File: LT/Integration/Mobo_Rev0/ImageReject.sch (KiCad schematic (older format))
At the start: 6 parts

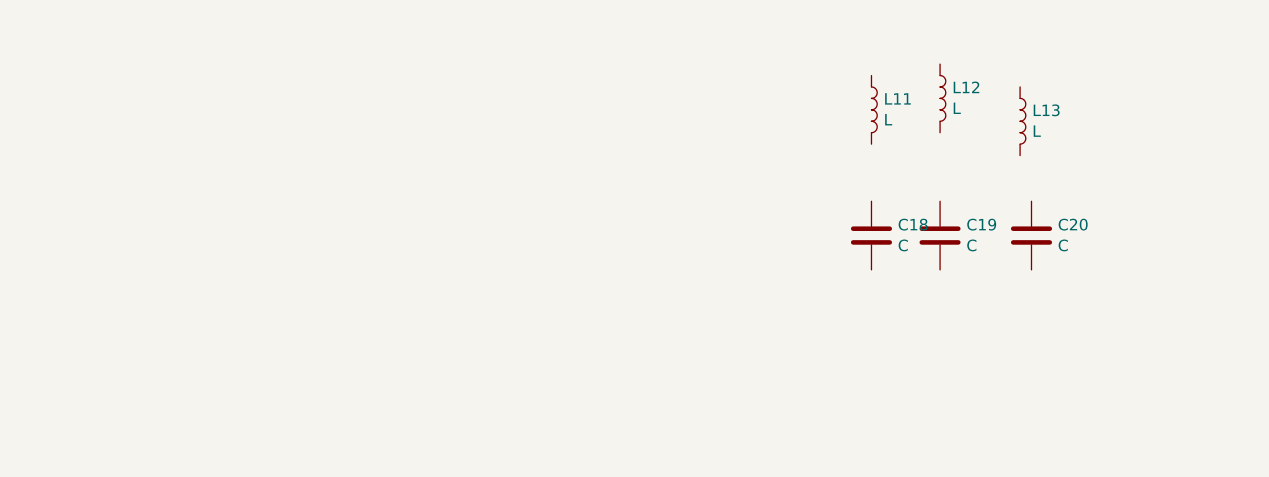
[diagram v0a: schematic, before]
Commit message: I uploaded the schematics for the receiving stage into their respective hierarchial sheets and have begun the integration of the received stage
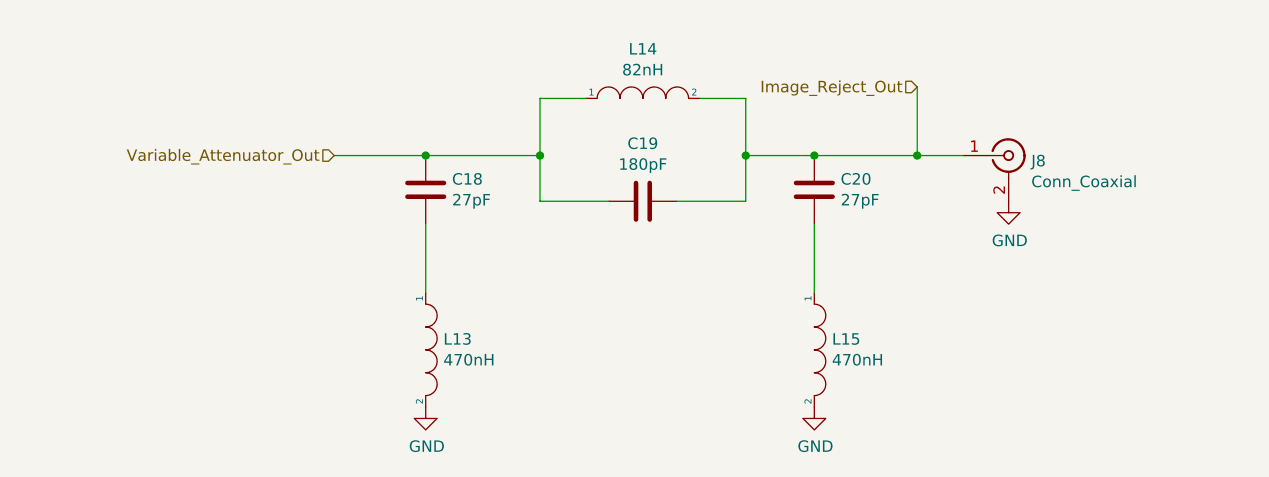
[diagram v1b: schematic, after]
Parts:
- removed L11, L12, L13: L, Inductor_SMD:L_0805_2012Metric, symbol Device:L
- added J8: Conn_Coaxial, Connector_Coaxial:SMA_Molex_73251-1153_EdgeMount_Horizontal, symbol Connector:Conn_Coaxial
- added L13, L15: 470nH, Inductor_SMD:L_0805_2012Metric_Pad1.15x1.40mm_HandSolder, symbol pspice:INDUCTOR
- added L14: 82nH, Inductor_SMD:L_0805_2012Metric_Pad1.15x1.40mm_HandSolder, symbol pspice:INDUCTOR
- C18, C20: value C -> 27pF; footprint Capacitor_SMD:C_0805_2012Metric -> Capacitor_SMD:C_0805_2012Metric_Pad1.15x1.40mm_HandSolder
- C19: value C -> 180pF; footprint Capacitor_SMD:C_0805_2012Metric -> Capacitor_SMD:C_0805_2012Metric_Pad1.15x1.40mm_HandSolder
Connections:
- net Variable_Attenuator_Out: now reaches C18.1
- net Variable_Attenuator_Out: now also C19.2, L14.1
- net at C18.2: now also L13.1
- net Image_Reject_Out: now reaches C19.1
- net Image_Reject_Out: now also C20.1, J8.1 (In), L14.2
- net at C20.2: now also L15.1
- new net GND: J8.2 (Ext), L13.2, L15.2
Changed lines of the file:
@@
 $EndDescr
 $Comp
-L Device:L L11
-U 1 1 5E4B3625
-P 4150 1900
-F 0 "L11" H 4203 1946 50  0000 L CNN
-F 1 "L" H 4203 1855 50  0000 L CNN
-F 2 "Inductor_SMD:L_0805_2012Metric" H 4150 1900 50  0001 C CNN
-F 3 "~" H 4150 1900 50  0001 C CNN
-	1    4150 1900
+L Device:C C18
+U 1 1 5CAD0F21
+P 2200 2250
+F 0 "C18" H 2315 2296 50  0000 L CNN
+F 1 "27pF" H 2315 2205 50  0000 L CNN
+F 2 "Capacitor_SMD:C_0805_2012Metric_Pad1.15x1.40mm_HandSolder" H 2238 2100 50  0001 C CNN
+F 3 "~" H 2200 2250 50  0001 C CNN
+	1    2200 2250
 	1    0    0    -1
 $EndComp
 $Comp
-L Device:L L12
-U 1 1 5E4B3675
-P 4450 1850
-F 0 "L12" H 4503 1896 50  0000 L CNN
-F 1 "L" H 4503 1805 50  0000 L CNN
-F 2 "Inductor_SMD:L_0805_2012Metric" H 4450 1850 50  0001 C CNN
-F 3 "~" H 4450 1850 50  0001 C CNN
-	1    4450 1850
-	1    0    0    -1
-$EndComp
-$Comp
-L Device:L L13
-U 1 1 5E4B36B4
-P 4800 1950
-F 0 "L13" H 4853 1996 50  0000 L CNN
-F 1 "L" H 4853 1905 50  0000 L CNN
-F 2 "Inductor_SMD:L_0805_2012Metric" H 4800 1950 50  0001 C CNN
-F 3 "~" H 4800 1950 50  0001 C CNN
-	1    4800 1950
-	1    0    0    -1
-$EndComp
-$Comp
-L Device:C C18
-U 1 1 5E4B36FA
-P 4150 2450
-F 0 "C18" H 4265 2496 50  0000 L CNN
-F 1 "C" H 4265 2405 50  0000 L CNN
-F 2 "Capacitor_SMD:C_0805_2012Metric" H 4188 2300 50  0001 C CNN
-F 3 "~" H 4150 2450 50  0001 C CNN
-	1    4150 2450
+L Device:C C20
+U 1 1 5CAD104E
+P 3900 2250
+F 0 "C20" H 4015 2296 50  0000 L CNN
+F 1 "27pF" H 4015 2205 50  0000 L CNN
+F 2 "Capacitor_SMD:C_0805_2012Metric_Pad1.15x1.40mm_HandSolder" H 3938 2100 50  0001 C CNN
+F 3 "~" H 3900 2250 50  0001 C CNN
+	1    3900 2250
 	1    0    0    -1
 $EndComp
 $Comp
 L Device:C C19
-U 1 1 5E4B3741
-P 4450 2450
-F 0 "C19" H 4565 2496 50  0000 L CNN
-F 1 "C" H 4565 2405 50  0000 L CNN
-F 2 "Capacitor_SMD:C_0805_2012Metric" H 4488 2300 50  0001 C CNN
-F 3 "~" H 4450 2450 50  0001 C CNN
-	1    4450 2450
+U 1 1 5CAD10AE
+P 3150 2300
+F 0 "C19" V 2898 2300 50  0000 C CNN
+F 1 "180pF" V 2989 2300 50  0000 C CNN
+F 2 "Capacitor_SMD:C_0805_2012Metric_Pad1.15x1.40mm_HandSolder" H 3188 2150 50  0001 C CNN
+F 3 "~" H 3150 2300 50  0001 C CNN
+	1    3150 2300
+	0    1    1    0
+$EndComp
+$Comp
+L pspice:INDUCTOR L14
+U 1 1 5CAD1149
+P 3150 1850
+F 0 "L14" H 3150 2065 50  0000 C CNN
+F 1 "82nH" H 3150 1974 50  0000 C CNN
+F 2 "Inductor_SMD:L_0805_2012Metric_Pad1.15x1.40mm_HandSolder" H 3150 1850 50  0001 C CNN
+F 3 "~" H 3150 1850 50  0001 C CNN
+	1    3150 1850
 	1    0    0    -1
 $EndComp
 $Comp
-L Device:C C20
-U 1 1 5E4B3780
-P 4850 2450
-F 0 "C20" H 4965 2496 50  0000 L CNN
-F 1 "C" H 4965 2405 50  0000 L CNN
-F 2 "Capacitor_SMD:C_0805_2012Metric" H 4888 2300 50  0001 C CNN
-F 3 "~" H 4850 2450 50  0001 C CNN
-	1    4850 2450
+L pspice:INDUCTOR L13
+U 1 1 5CAD11AF
+P 2200 2950
+F 0 "L13" V 2154 3027 50  0000 L CNN
+F 1 "470nH" V 2245 3027 50  0000 L CNN
+F 2 "Inductor_SMD:L_0805_2012Metric_Pad1.15x1.40mm_HandSolder" H 2200 2950 50  0001 C CNN
+F 3 "~" H 2200 2950 50  0001 C CNN
+	1    2200 2950
+	0    1    1    0
+$EndComp
+$Comp
+L pspice:INDUCTOR L15
+U 1 1 5CAD1219
+P 3900 2950
+F 0 "L15" V 3854 3027 50  0000 L CNN
+F 1 "470nH" V 3945 3027 50  0000 L CNN
+F 2 "Inductor_SMD:L_0805_2012Metric_Pad1.15x1.40mm_HandSolder" H 3900 2950 50  0001 C CNN
+F 3 "~" H 3900 2950 50  0001 C CNN
+	1    3900 2950
+	0    1    1    0
+$EndComp
+Wire Wire Line
+	2200 2400 2200 2700
+Wire Wire Line
+	3900 2400 3900 2700
+Wire Wire Line
+	2200 2100 2700 2100
+Wire Wire Line
+	2700 2100 2700 1850
+Wire Wire Line
+	2700 1850 2900 1850
+Wire Wire Line
+	2700 2100 2700 2300
+Wire Wire Line
+	2700 2300 3000 2300
+Connection ~ 2700 2100
+Wire Wire Line
+	3300 2300 3600 2300
+Wire Wire Line
+	3600 2300 3600 2100
+Wire Wire Line
+	3600 1850 3400 1850
+Wire Wire Line
+	3600 2100 3900 2100
+Connection ~ 3600 2100
+Wire Wire Line
+	3600 2100 3600 1850
+$Comp
+L power:GND #PWR012
+U 1 1 5CAD1657
+P 3900 3200
+F 0 "#PWR012" H 3900 2950 50  0001 C CNN
+F 1 "GND" H 3905 3027 50  0000 C CNN
+F 2 "" H 3900 3200 50  0001 C CNN
+F 3 "" H 3900 3200 50  0001 C CNN
+	1    3900 3200
 	1    0    0    -1
 $EndComp
+$Comp
+L power:GND #PWR011
+U 1 1 5CAD1681
+P 2200 3200
+F 0 "#PWR011" H 2200 2950 50  0001 C CNN
+F 1 "GND" H 2205 3027 50  0000 C CNN
+F 2 "" H 2200 3200 50  0001 C CNN
+F 3 "" H 2200 3200 50  0001 C CNN
+	1    2200 3200
+	1    0    0    -1
+$EndComp
+Connection ~ 2200 2100
+$Comp
+L Connector:Conn_Coaxial J8
+U 1 1 5CAD1901
+P 4750 2100
+F 0 "J8" H 4849 2076 50  0000 L CNN
+F 1 "Conn_Coaxial" H 4849 1985 50  0000 L CNN
+F 2 "Connector_Coaxial:SMA_Molex_73251-1153_EdgeMount_Horizontal" H 4750 2100 50  0001 C CNN
+F 3 " ~" H 4750 2100 50  0001 C CNN
+	1    4750 2100
+	1    0    0    -1
+$EndComp
+Connection ~ 3900 2100
+$Comp
+L power:GND #PWR013
+U 1 1 5CAD1A24
+P 4750 2300
+F 0 "#PWR013" H 4750 2050 50  0001 C CNN
+F 1 "GND" H 4755 2127 50  0000 C CNN
+F 2 "" H 4750 2300 50  0001 C CNN
+F 3 "" H 4750 2300 50  0001 C CNN
+	1    4750 2300
+	1    0    0    -1
+$EndComp
+Wire Wire Line
+	3900 2100 4350 2100
+Wire Wire Line
+	1800 2100 2200 2100
+Text HLabel 1800 2100 0    50   Input ~ 0
+Variable_Attenuator_Out
+Text HLabel 4350 1800 0    50   Input ~ 0
+Image_Reject_Out
+Wire Wire Line
+	4350 1800 4350 2100
+Connection ~ 4350 2100
+Wire Wire Line
+	4350 2100 4550 2100
 $EndSCHEMATC

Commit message: Finished a preliminary layout for the Receiving Stage, and uploaded the schematics for the Pre-Amp, 29.4 BPF, and 29.4 LPF.
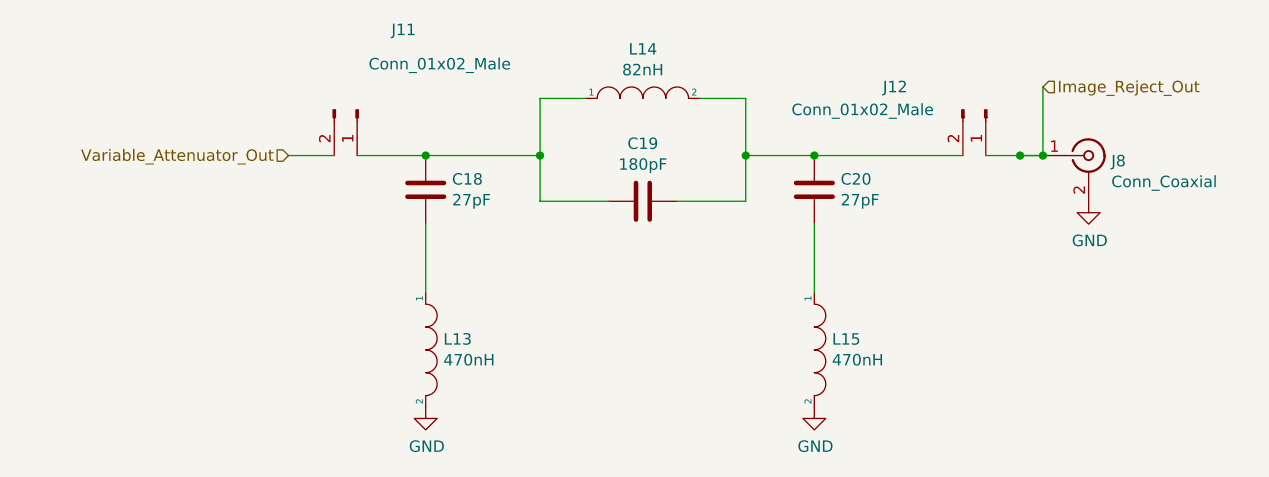
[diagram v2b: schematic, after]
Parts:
- added J11, J12: Conn_01x02_Male, Connector_PinHeader_2.54mm:PinHeader_1x02_P2.54mm_Vertical, symbol Connector:Conn_01x02_Male
- J8: footprint Connector_Coaxial:SMA_Molex_73251-1153_EdgeMount_Horizontal -> Connector_Coaxial:SMA_Amphenol_132289_EdgeMount
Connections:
- net Image_Reject_Out: now also J12.1 (Pin_1); no longer C19.1, C20.1, L14.2
- net Variable_Attenuator_Out: now also J11.2 (Pin_2); no longer C18.1, C19.2, L14.1
- new net: C18.1, C19.2, J11.1 (Pin_1), L14.1
- new net: C19.1, C20.1, J12.2 (Pin_2), L14.2
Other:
- moved on the sheet: J8
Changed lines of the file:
@@
 	1    0    0    -1
 $EndComp
-Connection ~ 2200 2100
 $Comp
 L Connector:Conn_Coaxial J8
 U 1 1 5CAD1901
-P 4750 2100
-F 0 "J8" H 4849 2076 50  0000 L CNN
-F 1 "Conn_Coaxial" H 4849 1985 50  0000 L CNN
-F 2 "Connector_Coaxial:SMA_Molex_73251-1153_EdgeMount_Horizontal" H 4750 2100 50  0001 C CNN
-F 3 " ~" H 4750 2100 50  0001 C CNN
-	1    4750 2100
+P 5100 2100
+F 0 "J8" H 5199 2076 50  0000 L CNN
+F 1 "Conn_Coaxial" H 5199 1985 50  0000 L CNN
+F 2 "Connector_Coaxial:SMA_Amphenol_132289_EdgeMount" H 5100 2100 50  0001 C CNN
+F 3 " ~" H 5100 2100 50  0001 C CNN
+	1    5100 2100
 	1    0    0    -1
 $EndComp
@@
 L power:GND #PWR013
 U 1 1 5CAD1A24
-P 4750 2300
-F 0 "#PWR013" H 4750 2050 50  0001 C CNN
-F 1 "GND" H 4755 2127 50  0000 C CNN
-F 2 "" H 4750 2300 50  0001 C CNN
-F 3 "" H 4750 2300 50  0001 C CNN
-	1    4750 2300
+P 5100 2300
+F 0 "#PWR013" H 5100 2050 50  0001 C CNN
+F 1 "GND" H 5105 2127 50  0000 C CNN
+F 2 "" H 5100 2300 50  0001 C CNN
+F 3 "" H 5100 2300 50  0001 C CNN
+	1    5100 2300
 	1    0    0    -1
 $EndComp
+Text HLabel 1600 2100 0    50   Input ~ 0
+Variable_Attenuator_Out
+Text HLabel 4900 1800 2    50   Input ~ 0
+Image_Reject_Out
+$Comp
+L Connector:Conn_01x02_Male J11
+U 1 1 5E8E6F64
+P 1900 1900
+F 0 "J11" V 1550 2050 50  0000 L CNN
+F 1 "Conn_01x02_Male" V 1700 1950 50  0000 L CNN
+F 2 "Connector_PinHeader_2.54mm:PinHeader_1x02_P2.54mm_Vertical" H 1900 1900 50  0001 C CNN
+F 3 "~" H 1900 1900 50  0001 C CNN
+	1    1900 1900
+	0    1    1    0
+$EndComp
 Wire Wire Line
-	3900 2100 4350 2100
+	1900 2100 2200 2100
+Connection ~ 2200 2100
 Wire Wire Line
-	1800 2100 2200 2100
-Text HLabel 1800 2100 0    50   Input ~ 0
-Variable_Attenuator_Out
-Text HLabel 4350 1800 0    50   Input ~ 0
-Image_Reject_Out
+	1600 2100 1800 2100
 Wire Wire Line
-	4350 1800 4350 2100
-Connection ~ 4350 2100
+	3900 2100 4550 2100
+$Comp
+L Connector:Conn_01x02_Male J12
+U 1 1 5E8E9A6B
+P 4650 1900
+F 0 "J12" V 4550 1450 50  0000 L CNN
+F 1 "Conn_01x02_Male" V 4650 1050 50  0000 L CNN
+F 2 "Connector_PinHeader_2.54mm:PinHeader_1x02_P2.54mm_Vertical" H 4650 1900 50  0001 C CNN
+F 3 "~" H 4650 1900 50  0001 C CNN
+	1    4650 1900
+	0    1    1    0
+$EndComp
 Wire Wire Line
-	4350 2100 4550 2100
+	4900 1800 4900 2100
+Connection ~ 4900 2100
+Connection ~ 4800 2100
+Wire Wire Line
+	4800 2100 4900 2100
+Wire Wire Line
+	4650 2100 4900 2100
 $EndSCHEMATC

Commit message: Uploaded Schematics to Integration of Phase 2
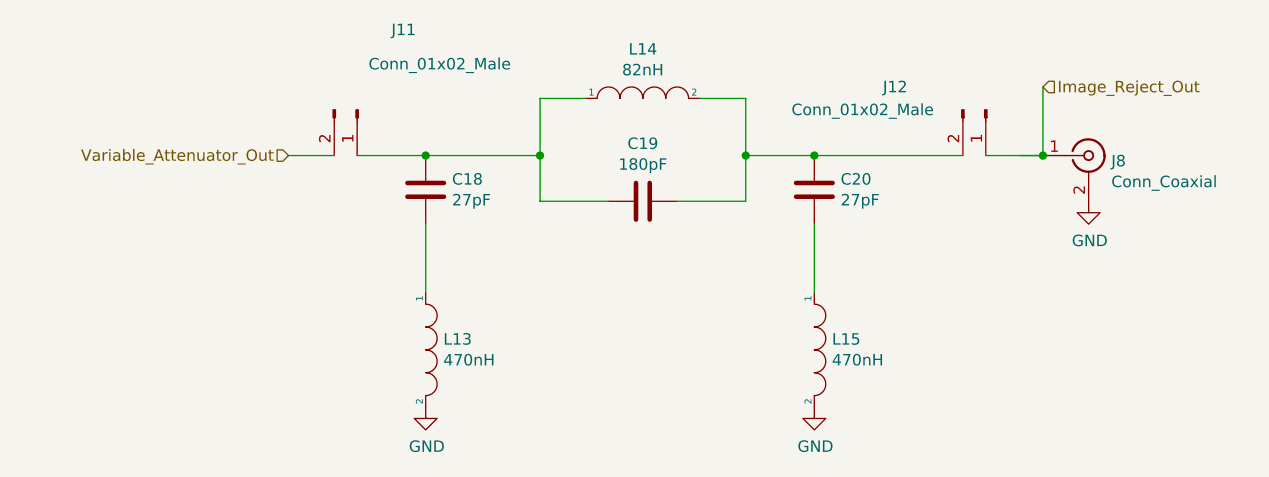
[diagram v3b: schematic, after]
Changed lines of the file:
@@
 EESchema Schematic File Version 4
-EELAYER 30 0
+LIBS:Mobo_Rev1-cache
+EELAYER 26 0
 EELAYER END
 $Descr A4 11693 8268
@@
 	4900 1800 4900 2100
 Connection ~ 4900 2100
-Connection ~ 4800 2100
 Wire Wire Line
 	4800 2100 4900 2100
